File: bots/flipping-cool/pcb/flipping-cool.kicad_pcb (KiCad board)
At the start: 2 copper layers, 140 x 110 mm, 36 parts, among them J1 XT30_BATTERY_IN_GNB4502S80AHV, J10 MATEK_ELRS_R24_P6_PWM, J11 R24_P6_VBAT_TELEMETRY_SENSE, J2 REMOVABLE_LINK_OR_RATED_SWITCH, J20 WEKA_POWER_INPUT_XT30, J21 WEKA_PWM_INPUTS_NAMED, J22 WEKA_MOTOR_OUTPUT_SOLDER_PADS, J23 MOTOR_FRONT_LEFT_POLOLU_3064, J24 MOTOR_REAR_LEFT_POLOLU_3064, J25 MOTOR_FRONT_RIGHT_POLOLU_3064, J26 MOTOR_REAR_RIGHT_POLOLU_3064, J3 VISIBLE_POWER_LED_CURRENT_LIM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, J30 SAVOX_SH0255MGP_FRONT_REAR_AX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, J31 SAVOX_SH0255MGP_LEFT_RIGHT_AX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, J4 2S_BALANCE_SENSE_NO_CHARGE, J5 POLOLU_D36V50F6_6V_5P5A_BEC

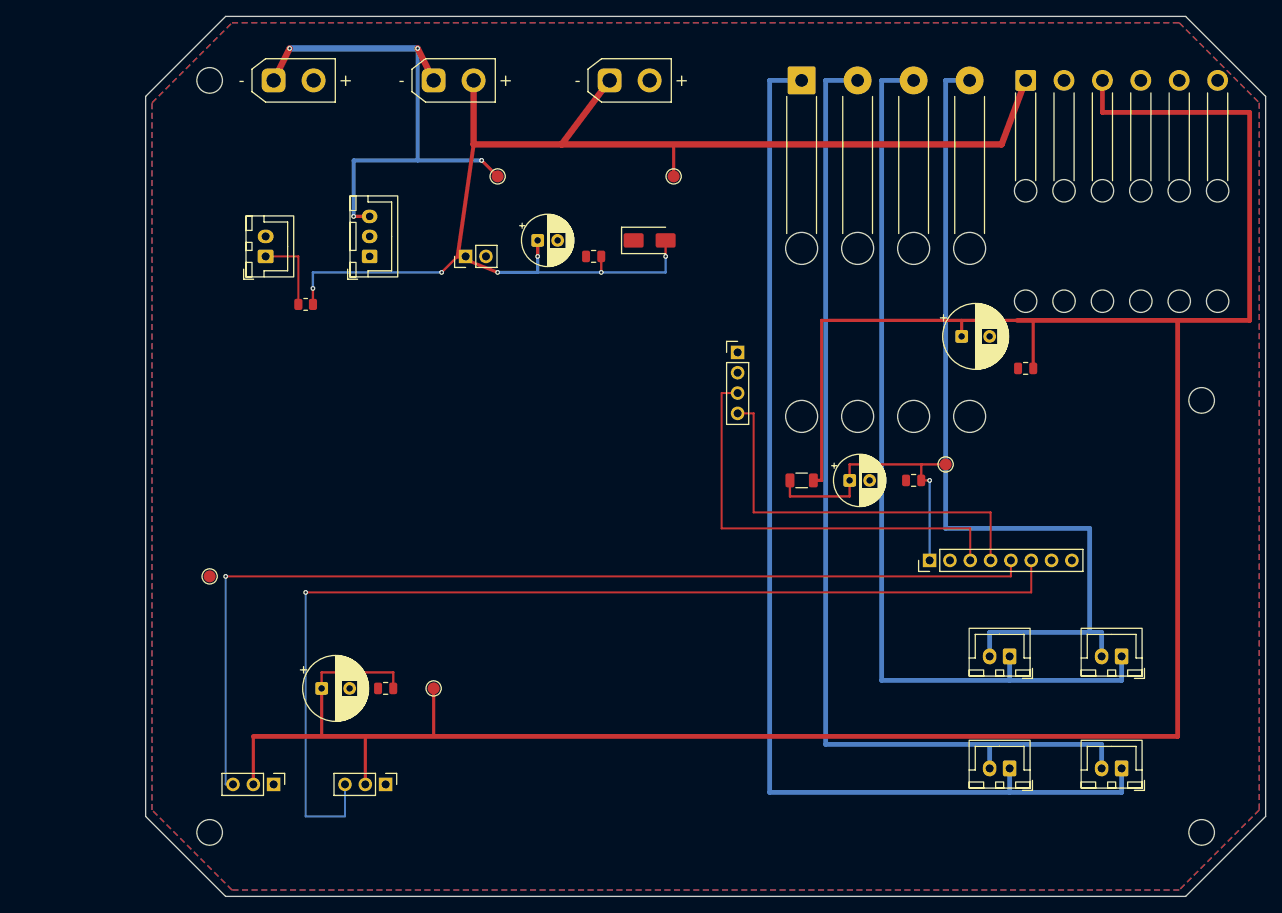
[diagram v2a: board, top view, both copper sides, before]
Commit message: Refactor Flipping Cool PCB design to Rev B, integrating active electrical features including ESP32-S3 module, power management, and control authority. Update documentation to reflect new architecture and validation requirements, while preserving Rev A historical context.
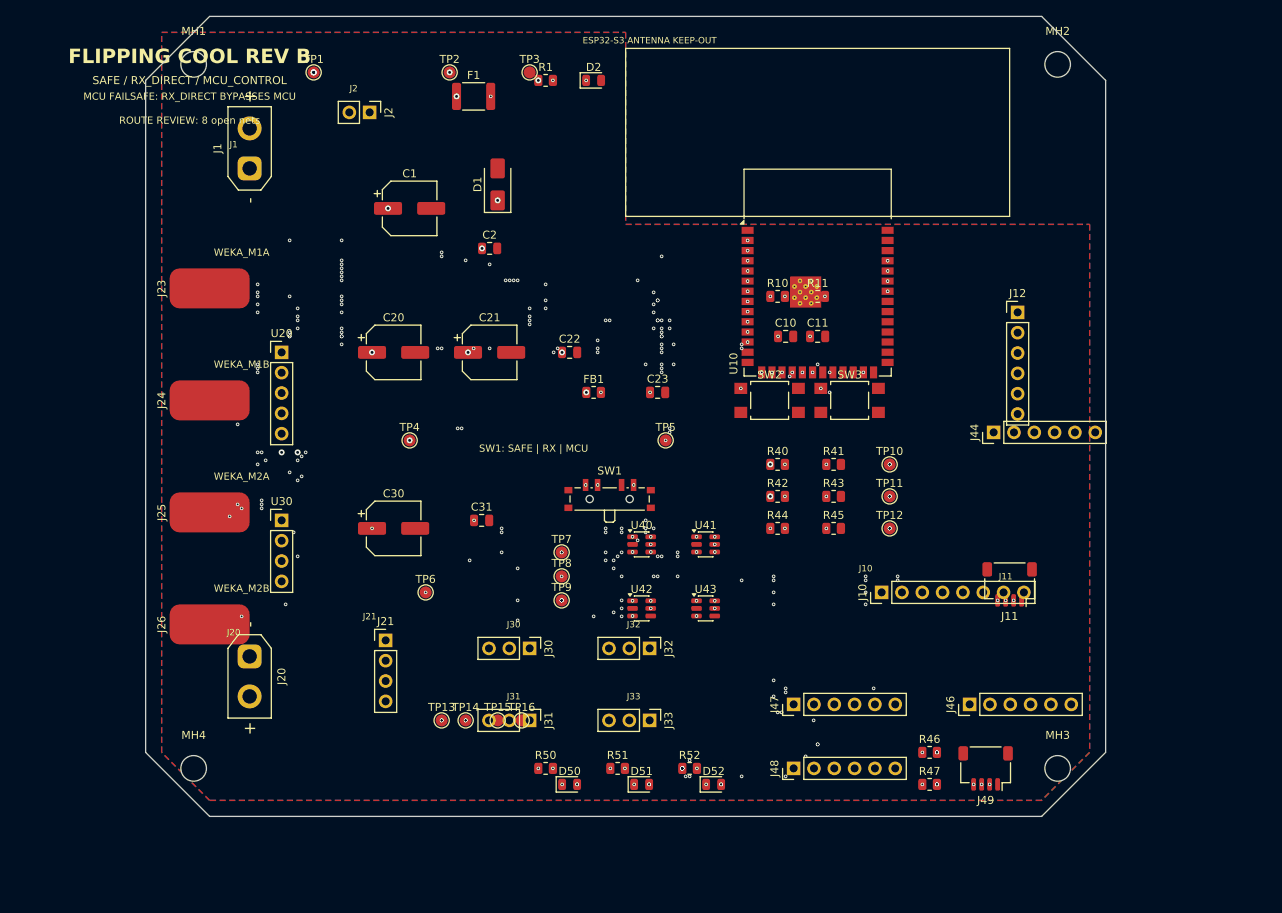
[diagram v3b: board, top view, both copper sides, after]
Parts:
- removed C3: 1000uF_10V_LOW_ESR, Capacitor_THT:CP_Radial_D8.0mm_P3.50mm
- removed C4: 100nF_10V, Capacitor_SMD:C_0805_2012Metric
- removed C5: 220uF_10V_RX, Capacitor_THT:CP_Radial_D6.3mm_P2.50mm
- removed C6: 100nF_RX, Capacitor_SMD:C_0805_2012Metric
- removed C7: 1000uF_SERVO_LOCAL, Capacitor_THT:CP_Radial_D8.0mm_P3.50mm
- removed C8: 100nF_SERVO_LOCAL, Capacitor_SMD:C_0805_2012Metric
- removed J22: WEKA_MOTOR_OUTPUT_SOLDER_PADS, Connector_Wire:SolderWire-0.75sqmm_1x04_P7mm_D1.25mm_OD3.5mm_Relief2x
- removed J3: VISIBLE_POWER_LED_CURRENT_LIMITED, Connector_JST:JST_XH_B2B-XH-A_1x02_P2.50mm_Vertical
- removed J4: 2S_BALANCE_SENSE_NO_CHARGE, Connector_JST:JST_XH_B3B-XH-A_1x03_P2.50mm_Vertical
- removed J5: POLOLU_D36V50F6_6V_5P5A_BEC, Connector_Wire:SolderWire-0.75sqmm_1x06_P4.8mm_D1.25mm_OD2.3mm_Relief2x
- added C10: 10uF_3V3_LOCAL, C_0805_2012Metric, F.Cu at (80.0, 40.0)
- added C11: 100nF_3V3_LOCAL, C_0805_2012Metric, F.Cu at (84.0, 40.0)
- added C20: 1000uF_10V_SERVO, CP_Elec_6.3x7.7, F.Cu at (31.0, 42.0)
- added C21: 100uF_10V, CP_Elec_6.3x7.7, F.Cu at (43.0, 42.0)
- added C22: 10uF_10V, C_0805_2012Metric, F.Cu at (53.0, 42.0)
- added C23: 22uF_RX, C_0805_2012Metric, F.Cu at (64.0, 47.0)
- added C30: 47uF_6V3, CP_Elec_6.3x7.7, F.Cu at (31.0, 64.0)
- added C31: 10uF_6V3, C_0805_2012Metric, F.Cu at (42.0, 63.0)
- added D2: PWR_LED, LED_0805_2012Metric, F.Cu at (56.0, 8.00)
- added D50: STATUS_LED, LED_0805_2012Metric, F.Cu at (53.0, 96.0)
- added D51: STATUS_LED, LED_0805_2012Metric, F.Cu at (62.0, 96.0)
- added D52: STATUS_LED, LED_0805_2012Metric, F.Cu at (71.0, 96.0)
- added F1: PTC_500mA_AUX, Fuse_1812_4532Metric, F.Cu at (41.0, 10.0)
- added J12: UART_PROGRAM, PinHeader_1x06_P2.54mm_Vertical, F.Cu at (109.0, 37.0)
- added J32: PWM_SERVO_SPARE1_SERVO, PinHeader_1x03_P2.54mm_Vertical, F.Cu at (63.0, 79.0)
- added J33: PWM_SERVO_SPARE2_SERVO, PinHeader_1x03_P2.54mm_Vertical, F.Cu at (63.0, 88.0)
- added J44: PIT_DEBUG, PinHeader_1x06_P2.54mm_Vertical, F.Cu at (106.0, 52.0)
- added J46: MCU_POWER_COMMS, PinHeader_1x06_P2.54mm_Vertical, F.Cu at (103.0, 86.0)
- added J47: MCU_SIGNAL_TAPS, PinHeader_1x06_P2.54mm_Vertical, F.Cu at (81.0, 86.0)
- added J48: MCU_SENSE_STATUS, PinHeader_1x06_P2.54mm_Vertical, F.Cu at (81.0, 94.0)
- added J49: I2C_STEMMA_QT, JST_SH_SM04B-SRSS-TB_1x04-1MP_P1.00mm_Horizontal, F.Cu at (105.0, 94.0)
- added R10: 10k_EN_PULLUP, R_0805_2012Metric, F.Cu at (79.0, 35.0)
- added R11: 10k_BOOT_PULLUP, R_0805_2012Metric, F.Cu at (84.0, 35.0)
- added R40: 100k, R_0805_2012Metric, F.Cu at (79.0, 56.0)
- added R41: 47k, R_0805_2012Metric, F.Cu at (86.0, 56.0)
- added R42: 100k, R_0805_2012Metric, F.Cu at (79.0, 60.0)
- added R43: 47k, R_0805_2012Metric, F.Cu at (86.0, 60.0)
- added R44: 100k, R_0805_2012Metric, F.Cu at (79.0, 64.0)
- added R45: 47k, R_0805_2012Metric, F.Cu at (86.0, 64.0)
- added R46: 4.7k_DNP, R_0805_2012Metric, F.Cu at (98.0, 92.0)
- added R47: 4.7k_DNP, R_0805_2012Metric, F.Cu at (98.0, 96.0)
- added R50: 330, R_0805_2012Metric, F.Cu at (50.0, 94.0)
- added R51: 330, R_0805_2012Metric, F.Cu at (59.0, 94.0)
- added R52: 330, R_0805_2012Metric, F.Cu at (68.0, 94.0)
- added SW1: MODE_SAFE_RX_MCU, SW_SP3T_PCM13, F.Cu at (58.0, 60.0)
- added SW2: RESET, SW_SPST_TL3305B, F.Cu at (78.0, 48.0)
- added SW3: BOOT, SW_SPST_TL3305B, F.Cu at (88.0, 48.0)
- added TP10: ADC_VBAT, TestPoint_Pad_D1.5mm, F.Cu at (93.0, 56.0)
- added TP11: ADC_SERVO_6V, TestPoint_Pad_D1.5mm, F.Cu at (93.0, 60.0)
- added TP12: ADC_RX_6V, TestPoint_Pad_D1.5mm, F.Cu at (93.0, 64.0)
- added TP13: PWM_DRIVE_LEFT, TestPoint_Pad_D1.5mm, F.Cu at (37.0, 88.0)
- added TP14: PWM_DRIVE_RIGHT, TestPoint_Pad_D1.5mm, F.Cu at (40.0, 88.0)
- added TP15: PWM_WEAPON_FR, TestPoint_Pad_D1.5mm, F.Cu at (44.0, 88.0)
- added TP16: PWM_WEAPON_LR, TestPoint_Pad_D1.5mm, F.Cu at (47.0, 88.0)
- added TP6: AUX_3V3, TestPoint_Pad_D1.5mm, F.Cu at (35.0, 72.0)
- added TP7: MODE_SAFE, TestPoint_Pad_D1.5mm, F.Cu at (52.0, 67.0)
- added TP8: MODE_RX_DIRECT, TestPoint_Pad_D1.5mm, F.Cu at (52.0, 70.0)
- added TP9: MODE_MCU_CONTROL, TestPoint_Pad_D1.5mm, F.Cu at (52.0, 73.0)
- added U10: ESP32-S3-WROOM-1, ESP32-S3-WROOM-1, F.Cu at (84.0, 32.0)
- added U20: 6V_BUCK_5.5A_MIN, PinHeader_1x05_P2.54mm_Vertical, F.Cu at (17.0, 42.0)
- added U30: 3V3_BUCK_POL_D24V5F3, PinHeader_1x04_P2.54mm_Vertical, F.Cu at (17.0, 63.0)
- added U40: SPDT_PWM_MUX_PWM_DRIVE_LEFT, SOT-23-6, F.Cu at (62.0, 66.0)
- added U41: SPDT_PWM_MUX_PWM_DRIVE_RIGHT, SOT-23-6, F.Cu at (70.0, 66.0)
- added U42: SPDT_PWM_MUX_PWM_WEAPON_FR, SOT-23-6, F.Cu at (62.0, 74.0)
- added U43: SPDT_PWM_MUX_PWM_WEAPON_LR, SOT-23-6, F.Cu at (70.0, 74.0)
- C1: footprint Capacitor_THT:CP_Radial_D6.3mm_P2.50mm -> CP_Elec_6.3x7.7
- C2: value 100nF_25V -> 10uF_16V; footprint Capacitor_SMD:C_0805_2012Metric -> C_0805_2012Metric
- D1: value SMAJ15CA_TVS -> SMBJ12CA_TVS; footprint Diode_SMD:D_SMA -> D_SMA
- FB1: value 0R_OR_FERRITE -> RX_6V_FILTER; footprint Resistor_SMD:R_1206_3216Metric -> R_0805_2012Metric
- J1: value XT30_BATTERY_IN_GNB4502S80AHV -> BATTERY_XT30; footprint Connector_AMASS:AMASS_XT30UPB-M_1x02_P5.0mm_Vertical -> AMASS_XT30UPB-F_1x02_P5.0mm_Vertical
- J10: footprint Connector_PinHeader_2.54mm:PinHeader_1x08_P2.54mm_Vertical -> PinHeader_1x08_P2.54mm_Vertical
- J11: value R24_P6_VBAT_TELEMETRY_SENSE -> CRSF_UART; footprint Connector_PinHeader_2.54mm:PinHeader_1x02_P2.54mm_Vertical -> JST_SH_SM04B-SRSS-TB_1x04-1MP_P1.00mm_Horizontal
- J2: value REMOVABLE_LINK_OR_RATED_SWITCH -> REMOVE_LINK_VBAT; footprint Connector_AMASS:AMASS_XT30UPB-F_1x02_P5.0mm_Vertical -> PinHeader_1x02_P2.54mm_Vertical
- J20: value WEKA_POWER_INPUT_XT30 -> WEKA_POWER_XT30; footprint Connector_AMASS:AMASS_XT30UPB-F_1x02_P5.0mm_Vertical -> AMASS_XT30UPB-F_1x02_P5.0mm_Vertical
- J21: value WEKA_PWM_INPUTS_NAMED -> WEKA_PWM; footprint Connector_PinHeader_2.54mm:PinHeader_1x04_P2.54mm_Vertical -> PinHeader_1x04_P2.54mm_Vertical
- J23: value MOTOR_FRONT_LEFT_POLOLU_3064 -> WEKA_M1A; footprint Connector_JST:JST_XH_B2B-XH-A_1x02_P2.50mm_Vertical -> SolderWirePad_1x01_SMD_5x10mm
- J24: value MOTOR_REAR_LEFT_POLOLU_3064 -> WEKA_M1B; footprint Connector_JST:JST_XH_B2B-XH-A_1x02_P2.50mm_Vertical -> SolderWirePad_1x01_SMD_5x10mm
- J25: value MOTOR_FRONT_RIGHT_POLOLU_3064 -> WEKA_M2A; footprint Connector_JST:JST_XH_B2B-XH-A_1x02_P2.50mm_Vertical -> SolderWirePad_1x01_SMD_5x10mm
- J26: value MOTOR_REAR_RIGHT_POLOLU_3064 -> WEKA_M2B; footprint Connector_JST:JST_XH_B2B-XH-A_1x02_P2.50mm_Vertical -> SolderWirePad_1x01_SMD_5x10mm
- J30: value SAVOX_SH0255MGP_FRONT_REAR_AXIS -> PWM_WEAPON_FR_SERVO; footprint Connector_PinHeader_2.54mm:PinHeader_1x03_P2.54mm_Vertical -> PinHeader_1x03_P2.54mm_Vertical
- J31: value SAVOX_SH0255MGP_LEFT_RIGHT_AXIS -> PWM_WEAPON_LR_SERVO; footprint Connector_PinHeader_2.54mm:PinHeader_1x03_P2.54mm_Vertical -> PinHeader_1x03_P2.54mm_Vertical
- MH1, MH2, MH3, MH4: value M3_NPTH -> M3 mounting
- R1: value 1k_LED_LIMIT -> 2.2k; footprint Resistor_SMD:R_0805_2012Metric -> R_0805_2012Metric
- TP1: value VBAT_RAW_TP -> VBAT_RAW; footprint TestPoint:TestPoint_Pad_D1.5mm -> TestPoint_Pad_D1.5mm
- TP2: value VBAT_SW_TP -> VBAT_SW; footprint TestPoint:TestPoint_Pad_D1.5mm -> TestPoint_Pad_D1.5mm
- TP3: value SERVO_6V_TP -> GND; footprint TestPoint:TestPoint_Pad_D1.5mm -> TestPoint_Pad_D1.5mm
- TP4: value RX_6V_TP -> SERVO_6V; footprint TestPoint:TestPoint_Pad_D1.5mm -> TestPoint_Pad_D1.5mm
- TP5: value GND_PWR_TP -> RX_6V; footprint TestPoint:TestPoint_Pad_D1.5mm -> TestPoint_Pad_D1.5mm
- moved J23 128.8 mm to (8.00, 34.0), turned to 90 degrees
- moved MH4 126.3 mm to (6.00, 94.0)
- moved J25 115.4 mm to (8.00, 62.0), turned to 90 degrees
- moved J24 110.1 mm to (8.00, 48.0), turned to 90 degrees
- moved MH3 106.3 mm to (114.0, 94.0)
- moved J26 100.1 mm to (8.00, 76.0), turned to 90 degrees
- moved J20 84.9 mm to (13.0, 80.0), turned to -90 degrees
- moved J11 79.4 mm to (108.0, 71.0), turned to 180 degrees
- moved TP3 77.9 mm to (48.0, 7.00)
- moved TP4 67.1 mm to (33.0, 53.0)
- moved TP5 59.5 mm to (65.0, 53.0)
- moved J21 56.9 mm to (30.0, 78.0)
- moved MH2 45.7 mm to (114.0, 6.00)
- moved R1 41.0 mm to (50.0, 8.00)
- moved J30 36.2 mm to (48.0, 79.0)
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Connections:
- net PWM_SPARE_5 renamed PWM_RX_SPARE1
- net PWM_SPARE_6 renamed PWM_RX_SPARE2
- net WEKA_5V_NC renamed WEKA_5V_BEC_NC_MON
- C2 pad 1: GND_PWR -> VBAT_SW
- C2 pad 2: VBAT_SW -> GND_PWR
- D1 pad 1: GND_PWR -> VBAT_SW
- D1 pad 2: VBAT_SW -> GND_PWR
- FB1 pad 1: RX_6V -> SERVO_6V
- FB1 pad 2: SERVO_6V -> RX_6V
- J10 pad 1: RX_6V -> GND_PWR
- J10 pad 2: GND_PWR -> RX_6V
- J10 pad 3: PWM_DRIVE_LEFT -> RX_PWM_DRIVE_LEFT
- J10 pad 4: PWM_DRIVE_RIGHT -> RX_PWM_DRIVE_RIGHT
- J10 pad 5: PWM_WEAPON_FR -> RX_PWM_WEAPON_FR
- J10 pad 6: PWM_WEAPON_LR -> RX_PWM_WEAPON_LR
- J11 pad 1: VBAT_SW -> GND_PWR
- J11 pad 2: GND_PWR -> RX_6V
- J24 pad 1: WEKA_M1A -> WEKA_M1B
- J26 pad 1: WEKA_M2A -> WEKA_M2B
- R1 pad 1: /01_battery_safety/PWR_LED_A -> VBAT_SW
- R1 pad 2: VBAT_SW -> PWR_LED_A
- TP3 pad 1: SERVO_6V -> GND_PWR
- TP4 pad 1: RX_6V -> SERVO_6V
- TP5 pad 1: GND_PWR -> RX_6V
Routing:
- net AUX_3V3: track 0.00 -> 1494.5 mm, vias 0 -> 50
- net VBAT_SW: track 173.0 -> 1002.0 mm, vias 6 -> 7
- net SERVO_6V: track 335.4 -> 901.0 mm, vias 0 -> 8
- net RX_6V: track 38.5 -> 358.0 mm, vias 1 -> 5
- net MODE_MCU_CONTROL: track 0.00 -> 280.5 mm, vias 0 -> 26
- net STATUS_LED_R_N: track 0.00 -> 265.5 mm, vias 0 -> 10
- net ADC_VBAT: track 0.00 -> 247.5 mm, vias 0 -> 13
- net ADC_SERVO_6V: track 0.00 -> 245.5 mm, vias 0 -> 13
- net I2C_SDA: track 0.00 -> 242.0 mm, vias 0 -> 12
- net ADC_RX_6V: track 0.00 -> 239.0 mm, vias 0 -> 12
- net I2C_SCL: track 0.00 -> 238.0 mm, vias 0 -> 9
- net STATUS_LED_G_N: track 0.00 -> 229.5 mm, vias 0 -> 12
- net STATUS_LED_B_N: track 0.00 -> 225.0 mm, vias 0 -> 11
- net MODE_SAFE: track 0.00 -> 185.0 mm, vias 0 -> 14
- net ESP_EN: track 0.00 -> 182.5 mm, vias 0 -> 8
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- added copper zone on In1.Cu, net GND_PWR
- added copper zone on In2.Cu, net GND_PWR
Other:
- board size 140 x 110 mm -> 120 x 100 mm
- copper layers 2 -> 4
- board text added: "ESP32-S3 ANTENNA KEEP-OUT"
- board text added: "FLIPPING COOL REV B"
- board text added: "J1"
- board text added: "J10"
- board text added: "J11"
- board text added: "J2"
- board text added: "J20"
- board text added: "J21"
- board text added: "J30"
- board text added: "J31"
- board text added: "J32"
- board text added: "J33"
- board text added: "MCU FAILSAFE: RX_DIRECT BYPASSES MCU"
- board text added: "ROUTE REVIEW: 8 open nets"
- board text added: "SAFE / RX_DIRECT / MCU_CONTROL"
- board text added: "SW1: SAFE | RX | MCU"
- board text added: "WEKA_M1A"
- board text added: "WEKA_M1B"
- board text added: "WEKA_M2A"
- board text added: "WEKA_M2B"

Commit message: Remove obsolete Flipping Cool Rev B project plan file and update schematic files to reflect the latest design changes, including integration of the ESP32-S3 module and enhancements to power management and control authority. Ensure all documentation is aligned with the current PCB design and architecture.
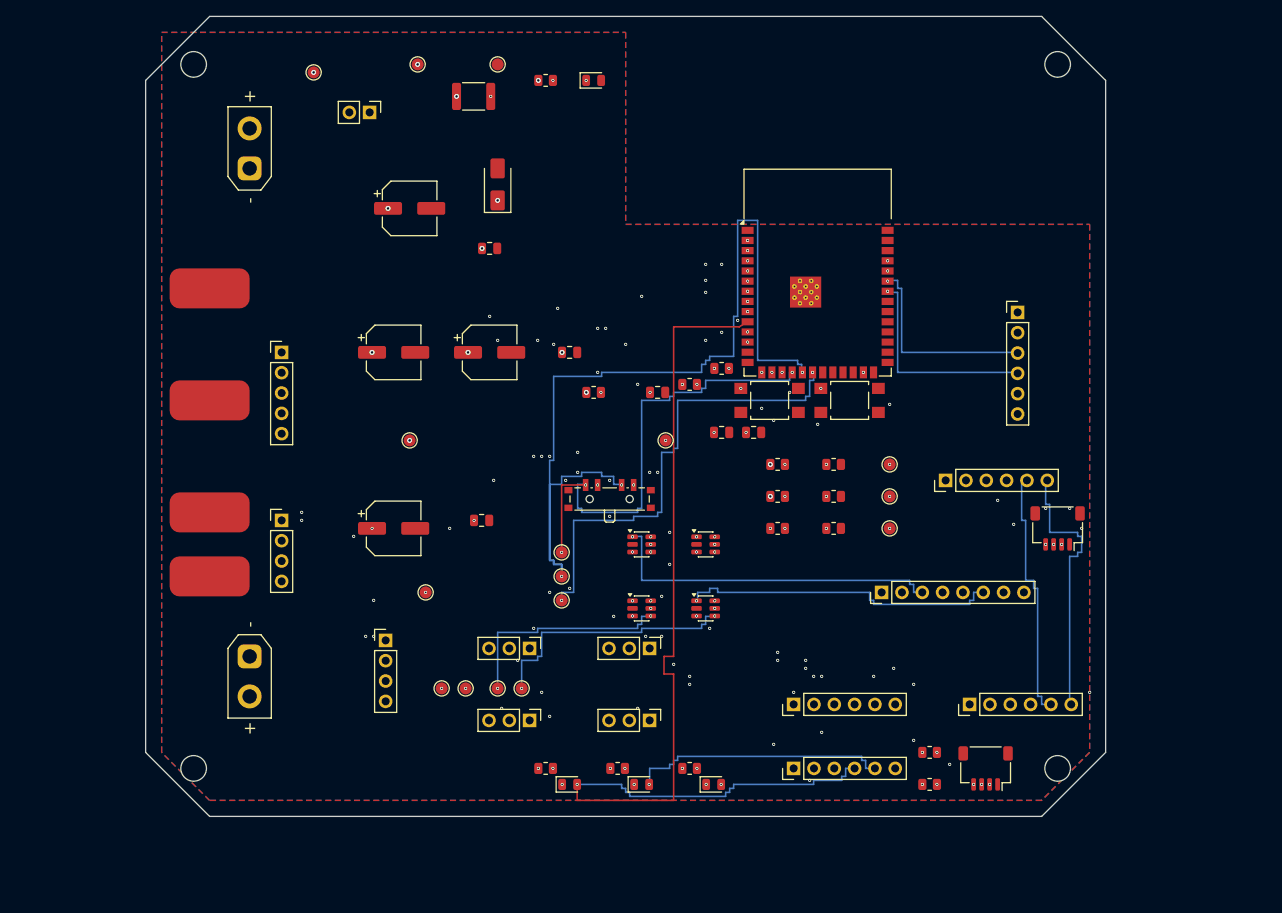
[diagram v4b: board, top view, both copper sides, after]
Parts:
- moved R11 19.4 mm to (68.0, 46.0)
- moved C10 14.4 mm to (72.0, 52.0)
- moved C11 14.4 mm to (76.0, 52.0)
- moved R10 11.4 mm to (72.0, 44.0)
- moved J11 9.22 mm to (114.0, 64.0)
- moved J44 8.49 mm to (100.0, 58.0)
- moved J26 6.00 mm to (8.00, 70.0)
- moved TP2 4.12 mm to (34.0, 6.00)
- moved TP3 4.12 mm to (44.0, 6.00)
- moved TP13 4.00 mm to (37.0, 84.0)
- moved TP14 4.00 mm to (40.0, 84.0)
- moved TP15 4.00 mm to (44.0, 84.0)
- moved TP16 4.00 mm to (47.0, 84.0)
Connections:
- J44 pad 1: GND_PWR -> VBAT_SW
- J44 pad 2: VBAT_SW -> GND_PWR
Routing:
- net AUX_3V3: track 1494.5 -> 341.5 mm, vias 50 -> 22
- net VBAT_SW: track 1002.0 -> 238.5 mm
- net SERVO_6V: track 901.0 -> 213.0 mm, vias 8 -> 6
- net RX_6V: track 358.0 -> 117.5 mm, vias 5 -> 7
- net RX_PWM_WEAPON_FR: track 65.0 -> 259.0 mm, vias 6 -> 5
- net PWM_WEAPON_LR: track 0.00 -> 180.5 mm, vias 0 -> 6
- net PWM_WEAPON_FR: track 0.00 -> 175.0 mm, vias 0 -> 4
- net UART0_TXD: track 166.0 -> 25.0 mm, vias 6 -> 1
- net STATUS_LED_R_N: track 265.5 -> 124.6 mm, vias 10 -> 1
- net UART0_RXD: track 162.0 -> 26.0 mm, vias 7 -> 1
- net ADC_VBAT: track 247.5 -> 125.5 mm, vias 13 -> 7
- net ADC_RX_6V: track 239.0 -> 128.0 mm, vias 12 -> 4
- net MODE_SAFE: track 185.0 -> 75.9 mm, vias 14 -> 3
- net ADC_SERVO_6V: track 245.5 -> 137.5 mm, vias 13 -> 8
- net ESP_EN: track 182.5 -> 80.7 mm, vias 8 -> 3
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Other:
- board text added: "ROUTE REVIEW: 1 open nets"
- board text removed: "ESP32-S3 ANTENNA KEEP-OUT"
- board text removed: "FLIPPING COOL REV B"
- board text removed: "J1"
- board text removed: "J10"
- board text removed: "J11"
- board text removed: "J2"
- board text removed: "J20"
- board text removed: "J21"
- board text removed: "J30"
- board text removed: "J31"
- board text removed: "J32"
- board text removed: "J33"
- board text removed: "MCU FAILSAFE: RX_DIRECT BYPASSES MCU"
- board text removed: "ROUTE REVIEW: 8 open nets"
- board text removed: "SAFE / RX_DIRECT / MCU_CONTROL"
